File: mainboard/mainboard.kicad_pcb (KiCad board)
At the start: 4 copper layers, 166.7 x 66.2 mm, 82 parts, among them J1 USB_C_Receptacle_USB2.0_16P, J10 Barrel_Jack, J2 Conn_01x03_Pin, J4 Conn_01x04_Socket, J5 Conn_01x04_Socket, J6 Screw_Terminal_01x02, J7 Conn_01x02_Socket, J8 Conn_01x02_Socket, J9 Conn_01x04_Socket, Q1 BTN8982TA, Q2 AO3400A, Q3 AO3400A, Q6 BTN8982TA, U1 ESP32-S3-WROOM-1, U2 USBLC6-2SC6, U3 AP2112K-3.3, U4 TPS2116DRL, U5 TPS62161DSG

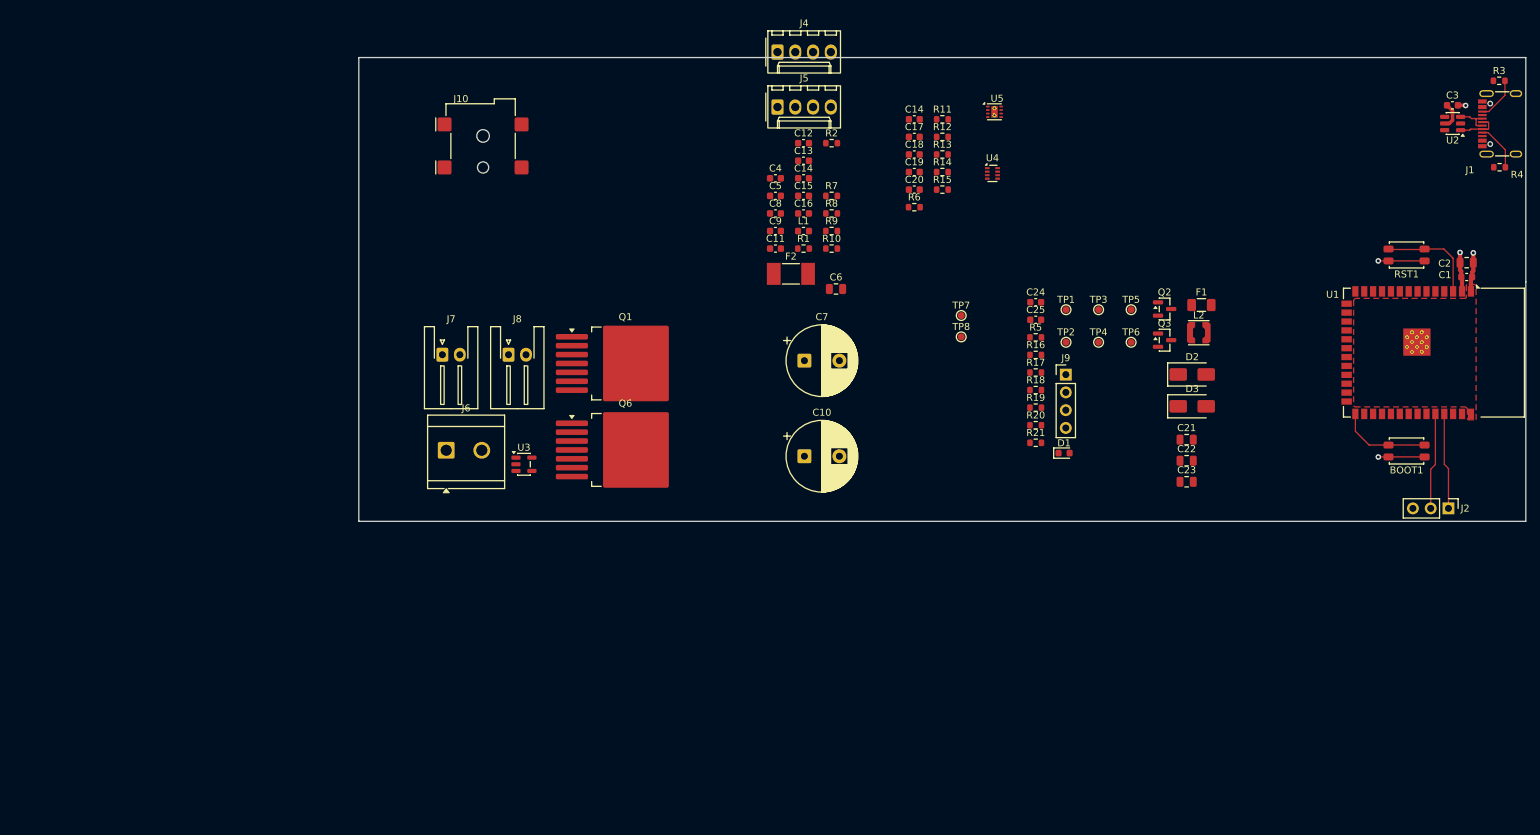
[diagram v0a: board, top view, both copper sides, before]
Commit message: worked on loadswitch layout, linear regulator layout
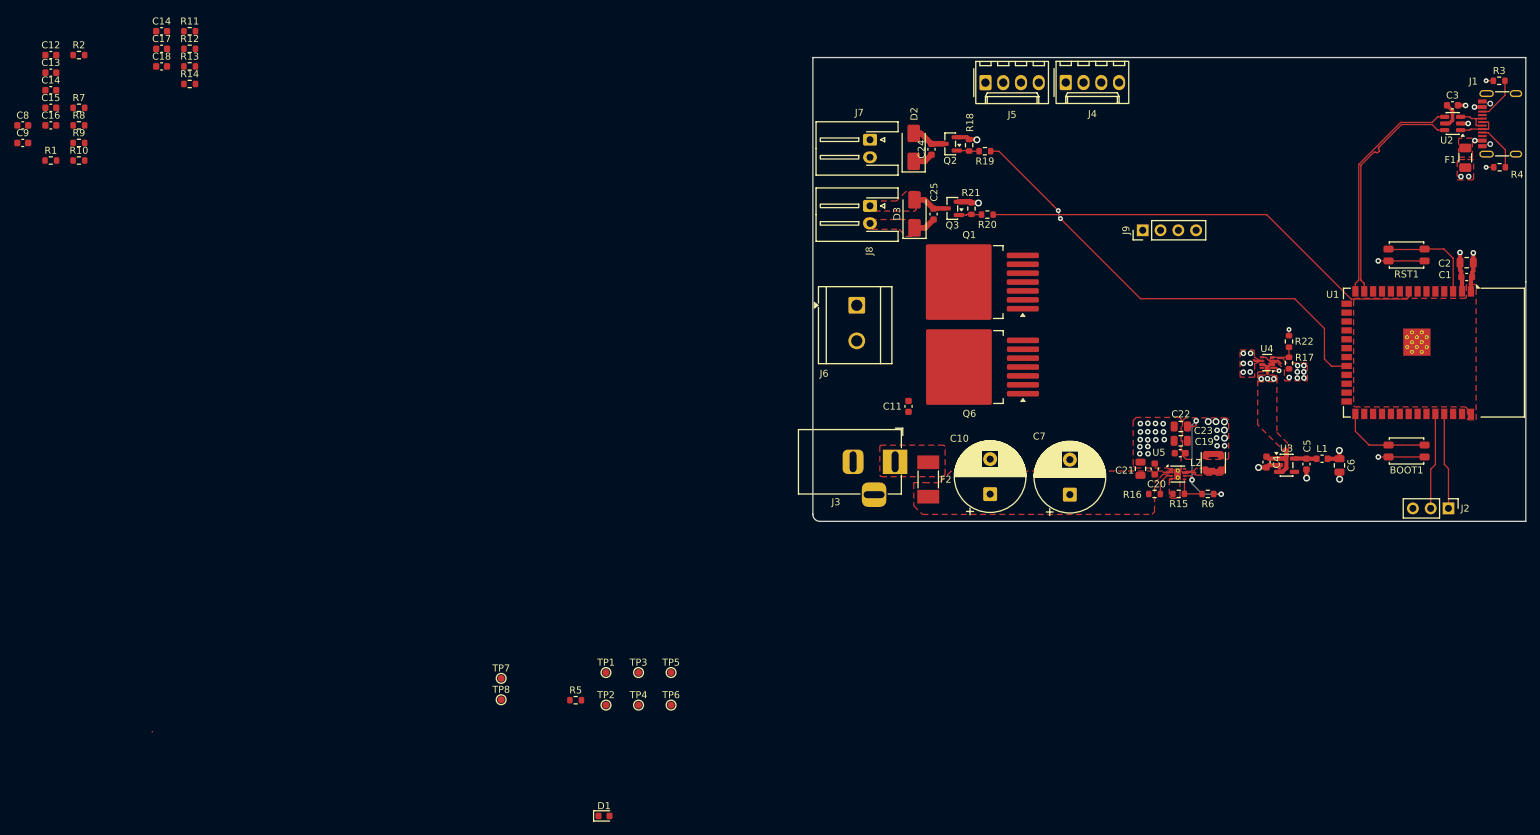
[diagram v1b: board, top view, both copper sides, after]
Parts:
- removed J10: Barrel_Jack, Connector_BarrelJack:BarrelJack_Wuerth_694108106102_2.5x5.5mm
- added J3: Barrel_Jack_MountingPin, Connector_BarrelJack:BarrelJack_Horizontal, F.Cu at (150.5, 107.5)
- added R22: 10k, Resistor_SMD:R_0603_1608Metric, F.Cu at (206.8, 90.4)
- R15: value 10k -> 52k3
- moved U3 108.9 mm to (206.4, 108.0)
- moved C8 108.3 mm to (25.9, 59.5)
- moved C9 108.3 mm to (25.9, 62.0)
- moved C12 108.3 mm to (29.9, 49.5)
- moved C13 108.3 mm to (29.9, 52.0)
- moved C14 108.3 mm to (45.7, 46.0)
- moved C14 108.3 mm to (29.9, 54.5)
- moved C15 108.3 mm to (29.9, 57.0)
- moved C16 108.3 mm to (29.9, 59.5)
- moved C17 108.3 mm to (45.7, 48.6)
- moved C18 108.3 mm to (45.7, 51.1)
- moved R1 108.3 mm to (29.9, 64.5)
- moved R10 108.3 mm to (33.9, 64.5)
- moved R11 108.3 mm to (49.7, 46.0)
- moved R12 108.3 mm to (49.7, 48.6)
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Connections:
- net Net-(U3-EN) renamed /5V_SEL
- net Net-(U4-PR1) renamed /PR1
- net Net-(U5-EN) renamed /EN
- net Net-(U5-FB) renamed /FB
- F2 pad 1: +12V -> /12V
- L2 pad 1: Net-(U5-SW) -> /SW
- U5 pad 6: Net-(U5-SW) -> +5V
- U5 pad 7: Net-(U5-SW) -> /SW
- U5 pad 8: GND -> unconnected-(U5-PG-Pad8)
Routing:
- net PWM3: track 0.00 -> 66.7 mm, vias 0 -> 2
- net PWM4: track 0.00 -> 65.3 mm
- net USB_D+: track 0.00 -> 33.4 mm
- net USB_D-: track 0.00 -> 33.4 mm
- net +5V: track 0.00 -> 22.2 mm, vias 0 -> 19
- net GND: track 20.0 -> 36.3 mm, vias 4 -> 30
- net /5V_SEL: track 0.00 -> 11.1 mm, vias 0 -> 3
- net +12V: track 0.00 -> 7.26 mm
- net /FAN_GND2: track 0.00 -> 5.20 mm
- net /FAN_GND: track 0.00 -> 4.90 mm
- net /FB: track 0.00 -> 4.60 mm
- net /PR1: track 0.00 -> 3.82 mm
- net /EN: track 0.00 -> 3.60 mm
- net /GATE2: track 0.00 -> 3.31 mm
- net Net-(U3-VOUT): track 0.00 -> 3.23 mm
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- added copper zone on F.Cu, net +12V
- added copper zone on F.Cu, net +5V
- added copper zone on F.Cu, net /12V
- added copper zone on F.Cu, net /5V_SEL
- added copper zone on F.Cu, net /FAN_GND2
- added copper zone on F.Cu, net /SW
- added copper zone on F.Cu, net /VBUS
- added copper zone on In2.Cu, net /VBUS
- added copper zone on F.Cu, net /VBUS_1
- added copper zone on In2.Cu, net /VBUS_1
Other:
- board size 166.7 x 66.2 mm -> 101.8 x 66.2 mm
